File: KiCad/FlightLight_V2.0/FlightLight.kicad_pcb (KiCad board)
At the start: 2 copper layers, 33.5 x 35.5 mm, 27 parts, among them J3 Conn_02x05_Odd_Even, SW1 AP, U2 ULN2003, U3 ESP-12F, U4 AMS1117-3.3

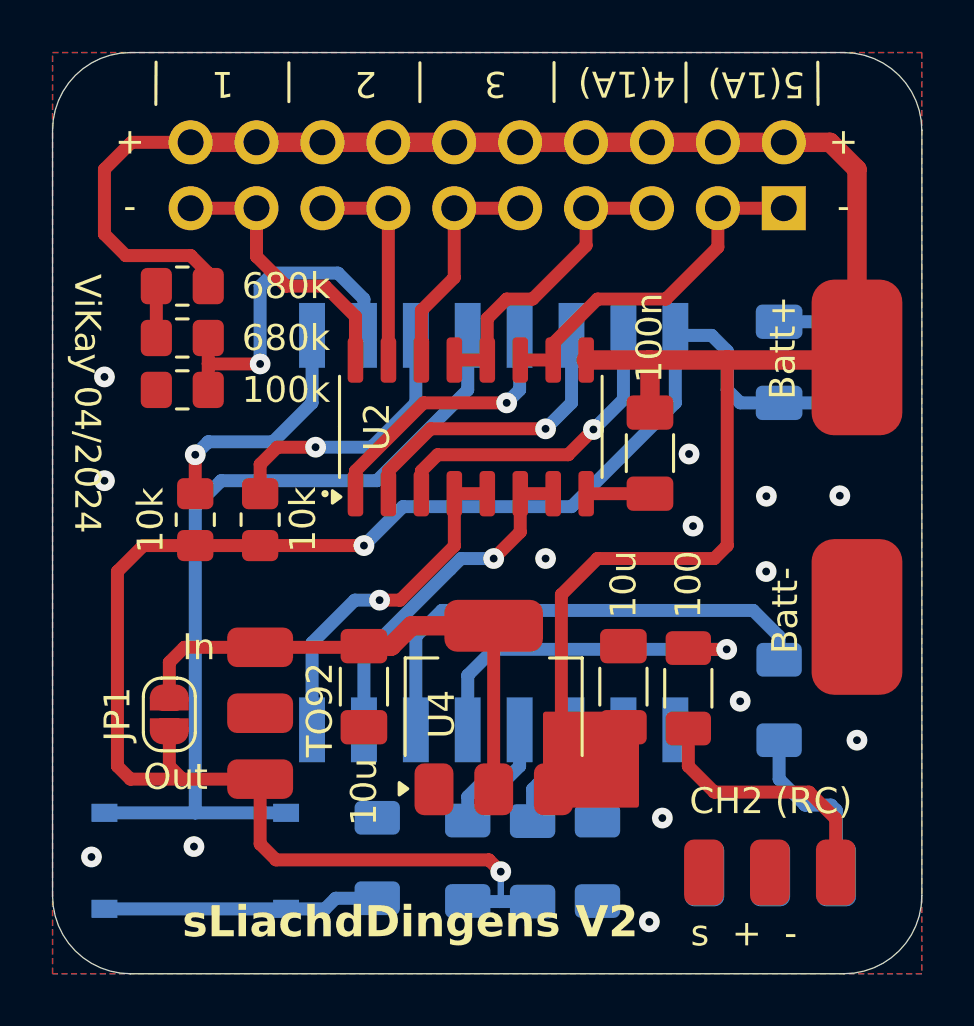
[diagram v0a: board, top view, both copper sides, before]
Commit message: Fix V2.1 - Pin TX nicht verwenden
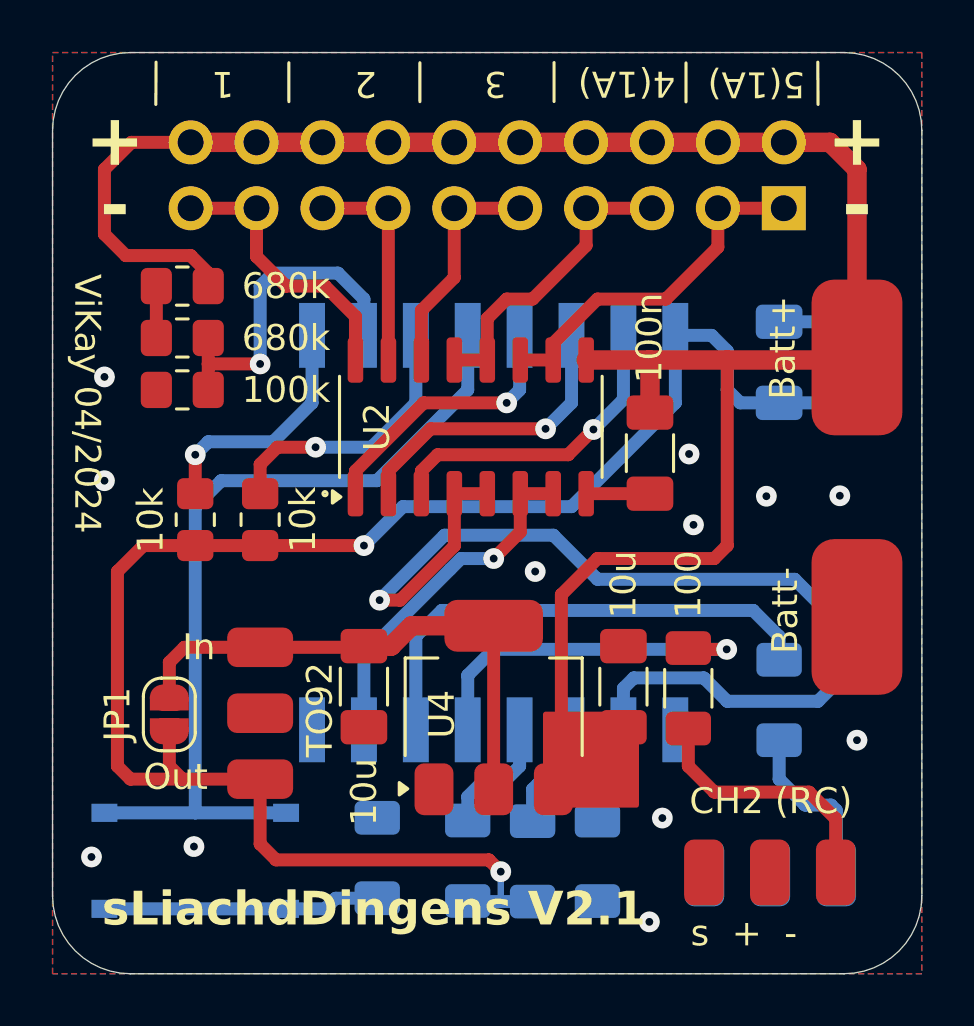
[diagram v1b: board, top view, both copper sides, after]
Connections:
- U2 pad 4: TX -> D8
- U2 pad 5: TX -> D8
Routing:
- net D8: track 3.91 -> 44.1 mm, vias 0 -> 1
- net TX: track 13.7 -> 0.00 mm, vias 1 -> 0
- net -BATT: vias 14 -> 12
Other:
- board text added: "AP: 1.2.3.4"
- board text added: "sLiachdDingens V2.1"
- board text removed: "AP:1.2.3.4"
- board text removed: "sLiachdDingens V2"
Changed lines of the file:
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@@
 			(layers "F.Cu" "F.Paste" "F.Mask")
 			(roundrect_rratio 0.25)
-			(net 17 "TX")
+			(net 15 "D8")
 			(pinfunction "I4")
 			(pintype "input")
@@
 			(layers "F.Cu" "F.Paste" "F.Mask")
 			(roundrect_rratio 0.25)
-			(net 17 "TX")
+			(net 15 "D8")
 			(pinfunction "I5")
 			(pintype "input")
@@
 	)
 	(gr_text "+"
-		(at 104.421691 64.428774 0)
+		(at 103.9 64.4 0)
 		(layer "B.SilkS")
 		(effects
 			(font
-				(size 1 1)
-				(thickness 0.153)
+				(size 2 2)
+				(thickness 0.4)
+				(bold yes)
 			)
 			(justify mirror)
@@
 	)
 	(gr_text "+"
-		(at 131.921691 64.428774 0)
+		(at 132.5 64.4 0)
 		(layer "B.SilkS")
 		(effects
 			(font
-				(size 1 1)
-				(thickness 0.153)
+				(size 2 2)
+				(thickness 0.4)
+				(bold yes)
 			)
 			(justify mirror)
@@
 	)
 	(gr_text "-"
-		(at 131.921691 66.928774 0)
+		(at 132.5 66.9 0)
 		(layer "B.SilkS")
 		(effects
 			(font
-				(size 1 1)
-				(thickness 0.153)
+				(size 2 2)
+				(thickness 0.4)
+				(bold yes)
 			)
 			(justify mirror)
@@
 	)
 	(gr_text "-"
-		(at 104.421691 66.928774 0)
+		(at 103.9 66.9 0)
 		(layer "B.SilkS")
 		(effects
 			(font
-				(size 1 1)
-				(thickness 0.153)
+				(size 2 2)
+				(thickness 0.3)
+				(bold yes)
 			)
 			(justify mirror)
@@
 		)
 	)
-	(gr_text "AP:1.2.3.4"
-		(at 131.172435 75.618665 90)
+	(gr_text "AP: 1.2.3.4"
+		(at 132.4 75.9 90)
 		(layer "B.SilkS" knockout)
 		(effects
 			(font
-				(size 1 1)
-				(thickness 0.153)
+				(size 1.2 1.2)
+				(thickness 0.24)
+				(bold yes)
 			)
 			(justify left bottom mirror)
@@
 	)
 	(gr_text "sLiachdDingens"
-		(at 133 75.5 90)
+		(at 133.5 75.7 90)
 		(layer "B.SilkS")
 		(effects
@@
 		)
 	)
-	(gr_text "sLiachdDingens V2"
-		(at 106.5 94.5 0)
+	(gr_text "sLiachdDingens V2.1"
+		(at 103.4 94 0)
 		(layer "F.SilkS" knockout)
 		(effects
 			(font
-				(size 1.2 1.2)
+				(size 1.3 1.3)
 				(thickness 0.2)
 				(bold yes)
@@
 	)
 	(gr_text "+"
-		(at 131.979129 64.427491 -0)
+		(at 132.5 64.4 0)
 		(layer "F.SilkS")
 		(effects
 			(font
-				(size 1 1)
-				(thickness 0.153)
+				(size 2 2)
+				(thickness 0.4)
+				(bold yes)
 			)
 		)
@@
 	)
 	(gr_text "-"
-		(at 131.979129 66.927491 -0)
+		(at 132.5 66.9 0)
 		(layer "F.SilkS")
 		(effects
 			(font
-				(size 1 1)
-				(thickness 0.153)
+				(size 2 2)
+				(thickness 0.4)
+				(bold yes)
 			)
 		)
 	)
 	(gr_text "+"
-		(at 104.479129 64.427491 -0)
+		(at 103.9 64.4 0)
 		(layer "F.SilkS")
 		(effects
 			(font
-				(size 1 1)
-				(thickness 0.153)
+				(size 2 2)
+				(thickness 0.4)
+				(bold yes)
 			)
 		)
 	)
 	(gr_text "-"
-		(at 104.479129 66.927491 -0)
+		(at 103.9 66.9 0)
 		(layer "F.SilkS")
 		(effects
 			(font
-				(size 1 1)
-				(thickness 0.153)
+				(size 2 2)
+				(thickness 0.4)
+				(bold yes)
 			)
 		)
@@
 	)
 	(via
-		(at 129 81)
-		(size 0.8)
-		(drill 0.3)
-		(layers "F.Cu" "B.Cu")
-		(free yes)
-		(net 1)
-	)
-	(via
-		(at 120.5 80.5)
+		(at 120.1 81)
 		(size 0.8)
 		(drill 0.3)
@@
 	)
 	(via
-		(at 126.182678 79.248795)
-		(size 0.8)
-		(drill 0.3)
-		(layers "F.Cu" "B.Cu")
-		(free yes)
-		(net 1)
-	)
-	(via
-		(at 128 86)
+		(at 126.2 79.2)
 		(size 0.8)
 		(drill 0.3)
@@
 	)
 	(segment
-		(start 123.5 87.1)
-		(end 123.5 88.5)
+		(start 116.98387 78)
+		(end 118.25387 78)
+		(width 0.5)
+		(layer "F.Cu")
+		(net 15)
+	)
+	(segment
+		(start 116.98387 80.01613)
+		(end 116.98387 78)
+		(width 0.5)
+		(layer "F.Cu")
+		(net 15)
+	)
+	(segment
+		(start 114.896718 82.103282)
+		(end 116.98387 80.01613)
+		(width 0.5)
+		(layer "F.Cu")
+		(net 15)
+	)
+	(segment
+		(start 114.10328 82.103282)
+		(end 114.896718 82.103282)
+		(width 0.5)
+		(layer "F.Cu")
+		(net 15)
+	)
+	(via
+		(at 114.10328 82.103282)
+		(size 0.8)
+		(drill 0.3)
+		(layers "F.Cu" "B.Cu")
+		(net 15)
+	)
+	(segment
+		(start 131 86)
+		(end 131.8 85.2)
 		(width 0.5)
 		(layer "B.Cu")
@@
 	)
 	(segment
-		(start 122.5 89.5)
-		(end 122.5 90.6)
+		(start 123.9 85.1)
+		(end 126.6 85.1)
 		(width 0.5)
 		(layer "B.Cu")
@@
 	)
 	(segment
-		(start 123.5 88.5)
-		(end 122.5 89.5)
+		(start 130.1 81.3)
+		(end 122.502082 81.3)
 		(width 0.5)
 		(layer "B.Cu")
@@
 	)
 	(segment
-		(start 117.991198 89.187393)
-		(end 117.5 89.678591)
+		(start 131.8 83)
+		(end 130.1 81.3)
 		(width 0.5)
 		(layer "B.Cu")
-		(net 16)
+		(net 15)
 	)
 	(segment
-		(start 119.5 88.5)
-		(end 118.812607 89.187393)
+		(start 123.5 85.5)
+		(end 123.9 85.1)
 		(width 0.5)
 		(layer "B.Cu")
-		(net 16)
+		(net 15)
 	)
 	(segment
-		(start 119.5 87.1)
-		(end 119.5 88.5)
+		(start 116.606562 79.6)
+		(end 114.10328 82.103282)
 		(width 0.5)
 		(layer "B.Cu")
-		(net 16)
+		(net 15)
 	)
 	(segment
-		(start 117.5 89.678591)
-		(end 117.5 90.596372)
+		(start 126.6 85.1)
+		(end 127.5 86)
 		(width 0.5)
 		(layer "B.Cu")
-		(net 16)
+		(net 15)
 	)
 	(segment
-		(start 118.812607 89.187393)
-		(end 117.991198 89.187393)
+		(start 122.502082 81.3)
+		(end 120.802082 79.6)
 		(width 0.5)
 		(layer "B.Cu")
-		(net 16)
+		(net 15)
 	)
 	(segment
-		(start 116.98387 78)
-		(end 118.25387 78)
+		(start 120.802082 79.6)
+		(end 116.606562 79.6)
 		(width 0.5)
-		(layer "F.Cu")
-		(net 17)
+		(layer "B.Cu")
+		(net 15)
 	)
 	(segment
-		(start 116.98387 80.01613)
-		(end 116.98387 78)
+		(start 123.5 87.1)
+		(end 123.5 88.5)
 		(width 0.5)
-		(layer "F.Cu")
-		(net 17)
+		(layer "B.Cu")
+		(net 15)
 	)
 	(segment
-		(start 114.896718 82.103282)
-		(end 116.98387 80.01613)
+		(start 123.5 87.1)
+		(end 123.5 85.5)
 		(width 0.5)
-		(layer "F.Cu")
-		(net 17)
+		(layer "B.Cu")
+		(net 15)
 	)
 	(segment
-		(start 114.10328 82.103282)
-		(end 114.896718 82.103282)
+		(start 122.5 89.5)
+		(end 122.5 90.6)
 		(width 0.5)
-		(layer "F.Cu")
-		(net 17)
+		(layer "B.Cu")
+		(net 15)
 	)
-	(via
-		(at 114.10328 82.103282)
-		(size 0.8)
-		(drill 0.3)
-		(layers "F.Cu" "B.Cu")
-		(net 17)
+	(segment
+		(start 131.8 85.2)
+		(end 131.8 83)
+		(width 0.5)
+		(layer "B.Cu")
+		(net 15)
+	)
+	(segment
+		(start 123.5 88.5)
+		(end 122.5 89.5)
+		(width 0.5)
+		(layer "B.Cu")
+		(net 15)
 	)
 	(segment
-		(start 113.146718 82.103282)
-		(end 111.5 83.75)
+		(start 127.5 86)
+		(end 131 86)
 		(width 0.5)
 		(layer "B.Cu")
-		(net 17)
+		(net 15)
 	)
 	(segment
-		(start 111.5 83.75)
-		(end 111.5 87.1)
+		(start 117.991198 89.187393)
+		(end 117.5 89.678591)
 		(width 0.5)
 		(layer "B.Cu")
-		(net 17)
+		(net 16)
 	)
 	(segment
-		(start 114.10328 82.103282)
-		(end 113.146718 82.103282)
+		(start 119.5 88.5)
+		(end 118.812607 89.187393)
 		(width 0.5)
 		(layer "B.Cu")
-		(net 17)
+		(net 16)
+	)
+	(segment
+		(start 119.5 87.1)
+		(end 119.5 88.5)
+		(width 0.5)
+		(layer "B.Cu")
+		(net 16)
+	)
+	(segment
+		(start 117.5 89.678591)
+		(end 117.5 90.596372)
+		(width 0.5)
+		(layer "B.Cu")
+		(net 16)
+	)
+	(segment
+		(start 118.812607 89.187393)
+		(end 117.991198 89.187393)
+		(width 0.5)
+		(layer "B.Cu")
+		(net 16)
 	)
 	(segment

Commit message: PCB V2.1
kleine Fixes
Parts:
- JP1: value kein Supervisor -> RST/EN; footprint Jumper:SolderJumper-2_P1.3mm_Open_RoundedPad1.0x1.5mm -> Jumper:SolderJumper-3_P1.3mm_Bridged12_RoundedPad1.0x1.5mm
- R7: footprint Resistor_SMD:R_1206_3216Metric_Pad1.30x1.75mm_HandSolder -> Resistor_SMD:R_0805_2012Metric_Pad1.20x1.40mm_HandSolder
- moved R3 10.7 mm to (109.3, 89.4), turned to 180 degrees
- moved R1 8.40 mm to (109.3, 87.4), turned to 180 degrees
- moved TO92 7.40 mm to (109.3, 76.5)
- moved JP1 1.28 mm to (105.0, 87.3), turned to 180 degrees
- moved R7 0.43 mm to (129.1, 86.1)
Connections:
- C4 pad 1: Net-(JP1-A) -> 3,3V
- JP1 pad 1: Net-(JP1-A) -> EN
- JP1 pad 2: 3,3V -> EN/RST
- R1 pad 2: Net-(U3-EN) -> EN
- R3 pad 2: Net-(U3-~{RST}) -> RST
- TO92 pad 1: Net-(JP1-A) -> +BATT
- TO92 pad 3: 3,3V -> EN/RST
- U3 pad 1: Net-(U3-~{RST}) -> RST
- U3 pad 3: Net-(U3-EN) -> EN
- U4 pad 2: Net-(JP1-A) -> 3,3V
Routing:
- net RST: track 0.00 -> 26.3 mm, vias 0 -> 1
- net EN: track 0.00 -> 21.5 mm, vias 0 -> 1
- net Net-(JP1-A): track 20.7 -> 0.00 mm
- net D8: track 44.1 -> 27.5 mm, vias 1 -> 3
- net Net-(U3-EN): track 10.7 -> 0.00 mm, vias 1 -> 0
- net +BATT: track 83.6 -> 93.3 mm
- net Net-(U3-~{RST}): track 9.43 -> 0.00 mm, vias 1 -> 0
- net EN/RST: track 0.00 -> 8.24 mm
- net 3,3V: track 66.5 -> 63.8 mm
- net /CH1: track 6.63 -> 7.20 mm
- net D1: track 19.3 -> 19.9 mm
- net -BATT: vias 12 -> 13
